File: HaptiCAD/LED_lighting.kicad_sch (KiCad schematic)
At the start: 35 parts, among them U201 SN74LV1T34DBV

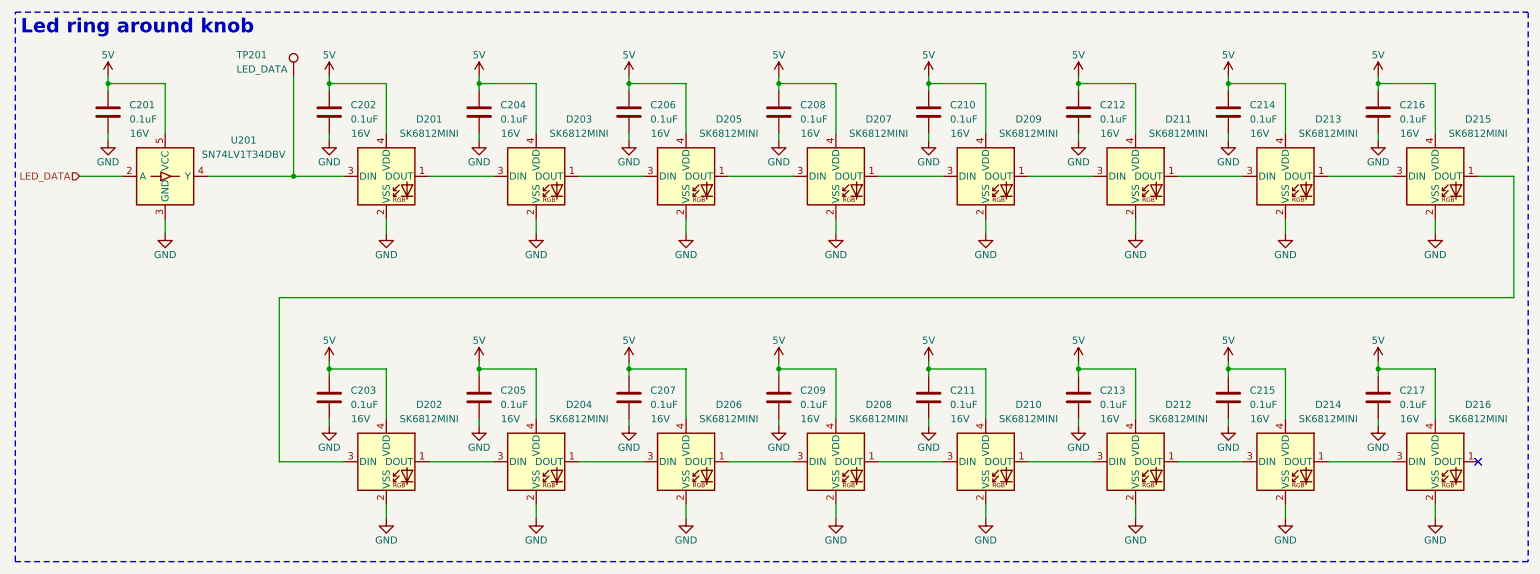
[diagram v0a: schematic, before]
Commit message: Updated name, schematic and pcb
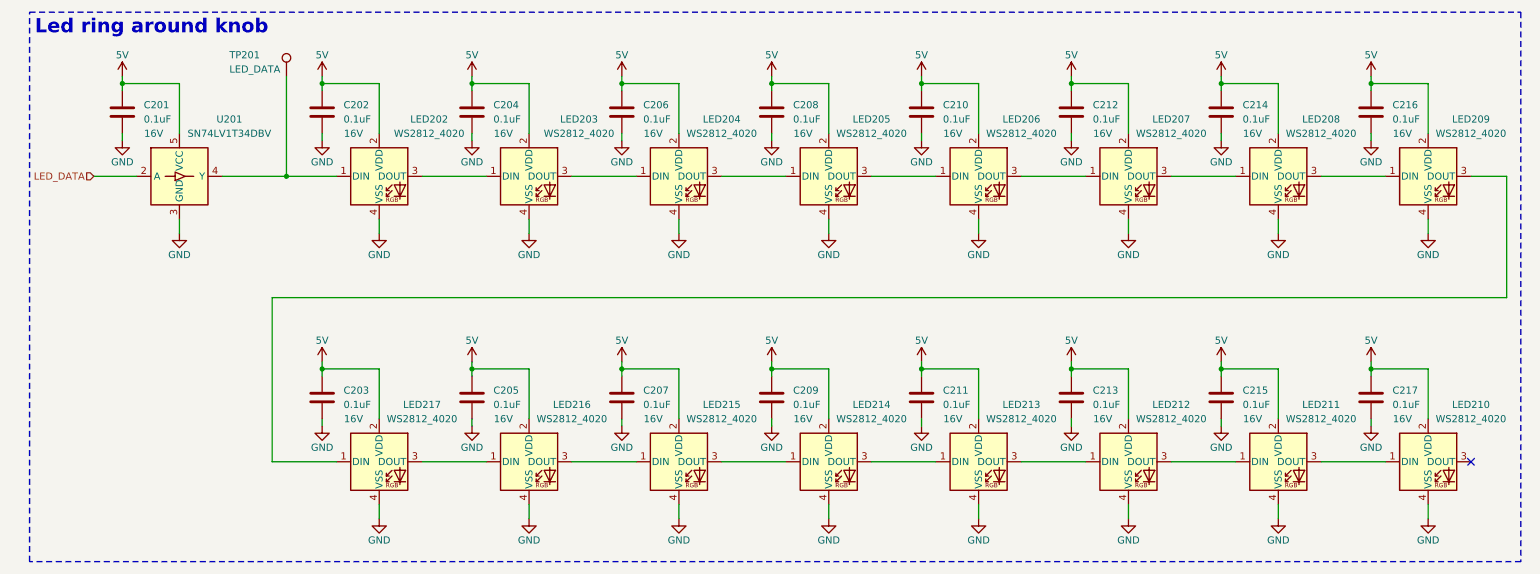
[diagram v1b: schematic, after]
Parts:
- removed D201, D202, D203, D204, D205, D206, D207, D208, D209, D210, D211, D212, D213, D214, D215, D216: SK6812MINI, LED_SMD:LED_SK6812MINI_PLCC4_3.5x3.5mm_P1.75mm, symbol LED:SK6812MINI
- added LED202, LED203, LED204, LED205, LED206, LED207, LED208, LED209, LED210, LED211, LED212, LED213, LED214, LED215, LED216, LED217: WS2812_4020, PCM_marbastlib-xp-various:LED_WS2812_4020, symbol PCM_marbastlib-various:WS2812_4020
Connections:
- net 5V: now also LED202.2 (VDD), LED203.2 (VDD), LED204.2 (VDD), LED205.2 (VDD), LED206.2 (VDD), LED207.2 (VDD), LED208.2 (VDD), LED209.2 (VDD), LED210.2 (VDD), LED211.2 (VDD), LED212.2 (VDD), LED213.2 (VDD), LED214.2 (VDD), LED215.2 (VDD), LED216.2 (VDD), LED217.2 (VDD)
- net GND: now also LED202.4 (VSS), LED203.4 (VSS), LED204.4 (VSS), LED205.4 (VSS), LED206.4 (VSS), LED207.4 (VSS), LED208.4 (VSS), LED209.4 (VSS), LED210.4 (VSS), LED211.4 (VSS), LED212.4 (VSS), LED213.4 (VSS), LED214.4 (VSS), LED215.4 (VSS), LED216.4 (VSS), LED217.4 (VSS)
- net at TP201.1, U201.4 (Y): now also LED202.1 (DIN)
- new net: LED211.1 (DIN), LED212.3 (DOUT)
- new net: LED210.1 (DIN), LED211.3 (DOUT)
- new net: LED209.3 (DOUT), LED217.1 (DIN)
- new net: LED216.1 (DIN), LED217.3 (DOUT)
- new net: LED203.3 (DOUT), LED204.1 (DIN)
- new net: LED204.3 (DOUT), LED205.1 (DIN)
- new net: LED205.3 (DOUT), LED206.1 (DIN)
- new net: LED206.3 (DOUT), LED207.1 (DIN)
- new net: LED213.1 (DIN), LED214.3 (DOUT)
- new net: LED212.1 (DIN), LED213.3 (DOUT)
- new net: LED207.3 (DOUT), LED208.1 (DIN)
- new net: LED202.3 (DOUT), LED203.1 (DIN)
- new net: LED215.1 (DIN), LED216.3 (DOUT)
- new net: LED214.1 (DIN), LED215.3 (DOUT)
- new net: LED208.3 (DOUT), LED209.1 (DIN)
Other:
- moved on the sheet: C201, C202, C203, C204, C205, C206, C207, C208, C209, C210, C211, C212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
